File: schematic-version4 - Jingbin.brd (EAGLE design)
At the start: 47 x 28 mm, 54 parts, among them J2 FTDI_DEVICE, M1 WIRELESS-NRF24L01, Q1 NX3225GD, T1 NMOS, T2 NMOS, T3 NMOS, T4 NMOS, U1 ATMEGA328P_TQFP, U2 GY-521MPU6050

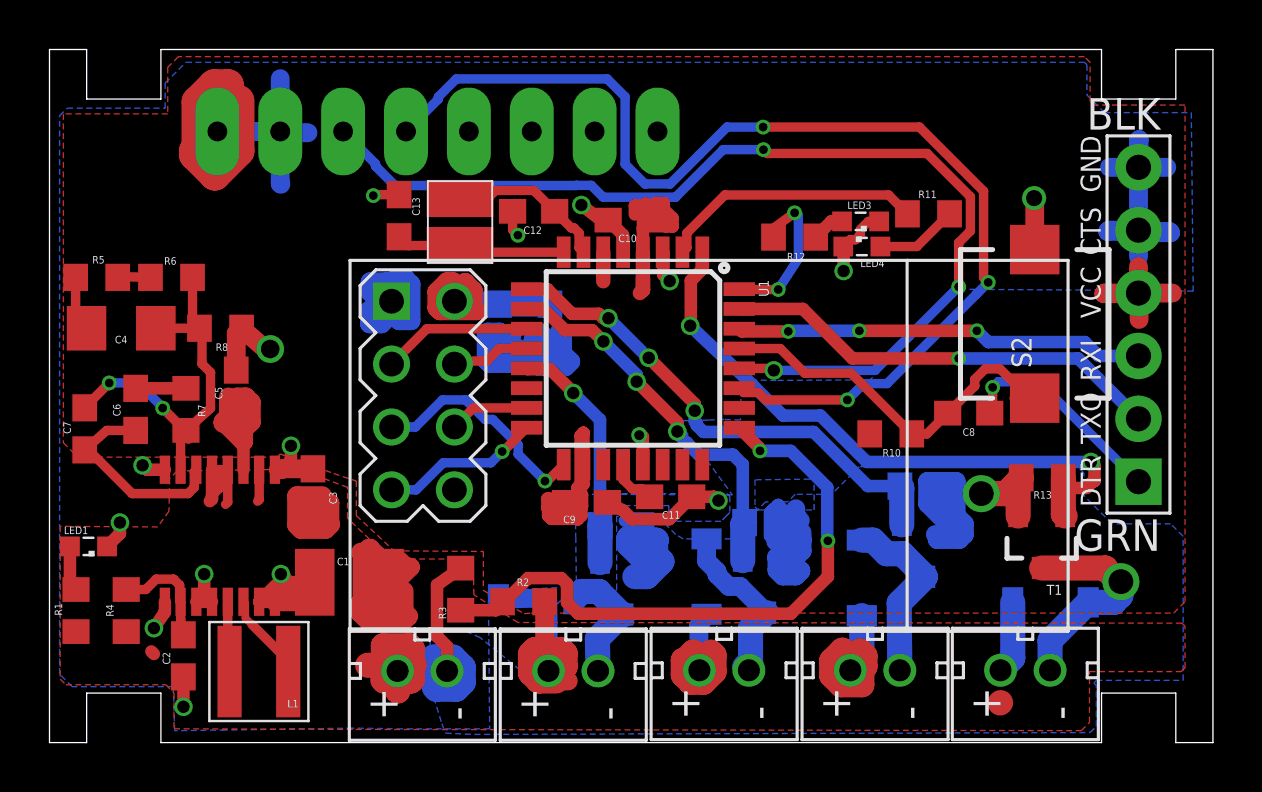
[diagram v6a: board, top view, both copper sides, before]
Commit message: More thicc paths
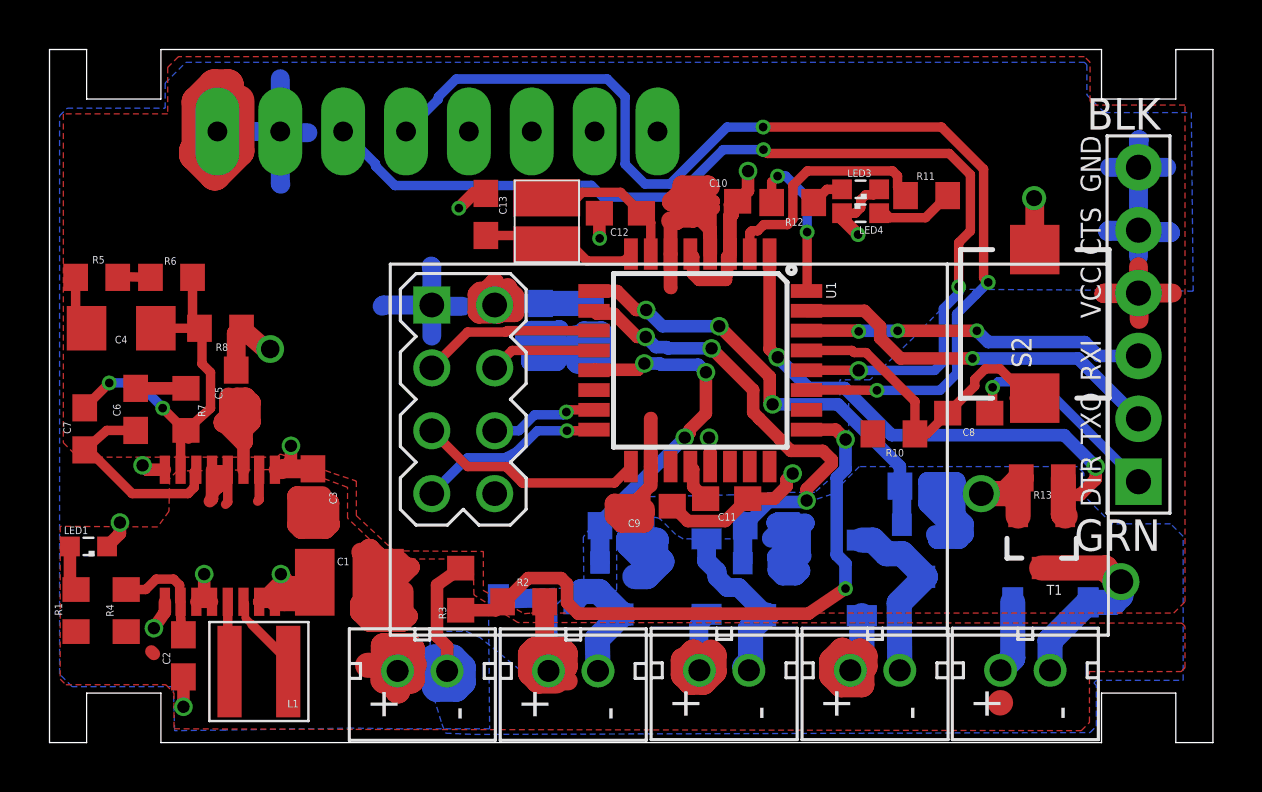
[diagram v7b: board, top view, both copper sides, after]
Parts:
- moved C10 3.61 mm to (26.9, 21.9), turned to 0 degrees
- moved C12 3.51 mm to (23.1, 21.4)
- moved C13 3.51 mm to (17.6, 21.3)
- moved Q1 3.51 mm to (20.1, 21.1)
- moved U1 2.72 mm to (26.3, 15.4)
- moved C9 2.62 mm to (24.3, 9.55)
- moved C11 2.26 mm to (27.4, 9.86)
- moved C15 1.68 mm to (21.9, 16.9)
- moved C14 1.65 mm to (19.8, 16.9)
- moved M1 1.63 mm to (28.1, 11.3)
- moved R12 1.40 mm to (30.0, 21.8)
- moved LED4 1.35 mm to (32.8, 21.4)
- moved LED3 1.30 mm to (32.8, 22.4)
- moved R11 0.74 mm to (35.4, 22.1)
- moved R15 0.13 mm to (29.0, 8.76)
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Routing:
- net PWM3: track 15.9 -> 21.1 mm
- net PWM4: track 11.2 -> 15.9 mm, vias 1 -> 3
- net PWM1: track 25.5 -> 22.6 mm
- net RXD: track 16.6 -> 13.9 mm
- net TXD: track 18.0 -> 15.5 mm
- net PWM2: track 20.4 -> 18.3 mm
- net N$2: track 15.9 -> 14.0 mm
- net V_REG_OUT: track 54.9 -> 56.7 mm
- net GND: track 113.8 -> 115.5 mm, vias 17 -> 16
- net SDA: track 45.6 -> 44.5 mm
- net MOSI: track 3.24 -> 4.36 mm, vias 0 -> 1
- net CSN: track 3.18 -> 4.31 mm
- net CE: track 6.05 -> 7.18 mm
- net MISO: track 6.50 -> 7.59 mm
- net DEBUG_LED2: track 10.7 -> 9.68 mm
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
